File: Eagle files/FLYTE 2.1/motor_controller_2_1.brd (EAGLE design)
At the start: 80 x 60 mm, 32 parts, among them J1 XT60-M, U1 MIC29302WU-TRTO-263-5_MCH-M

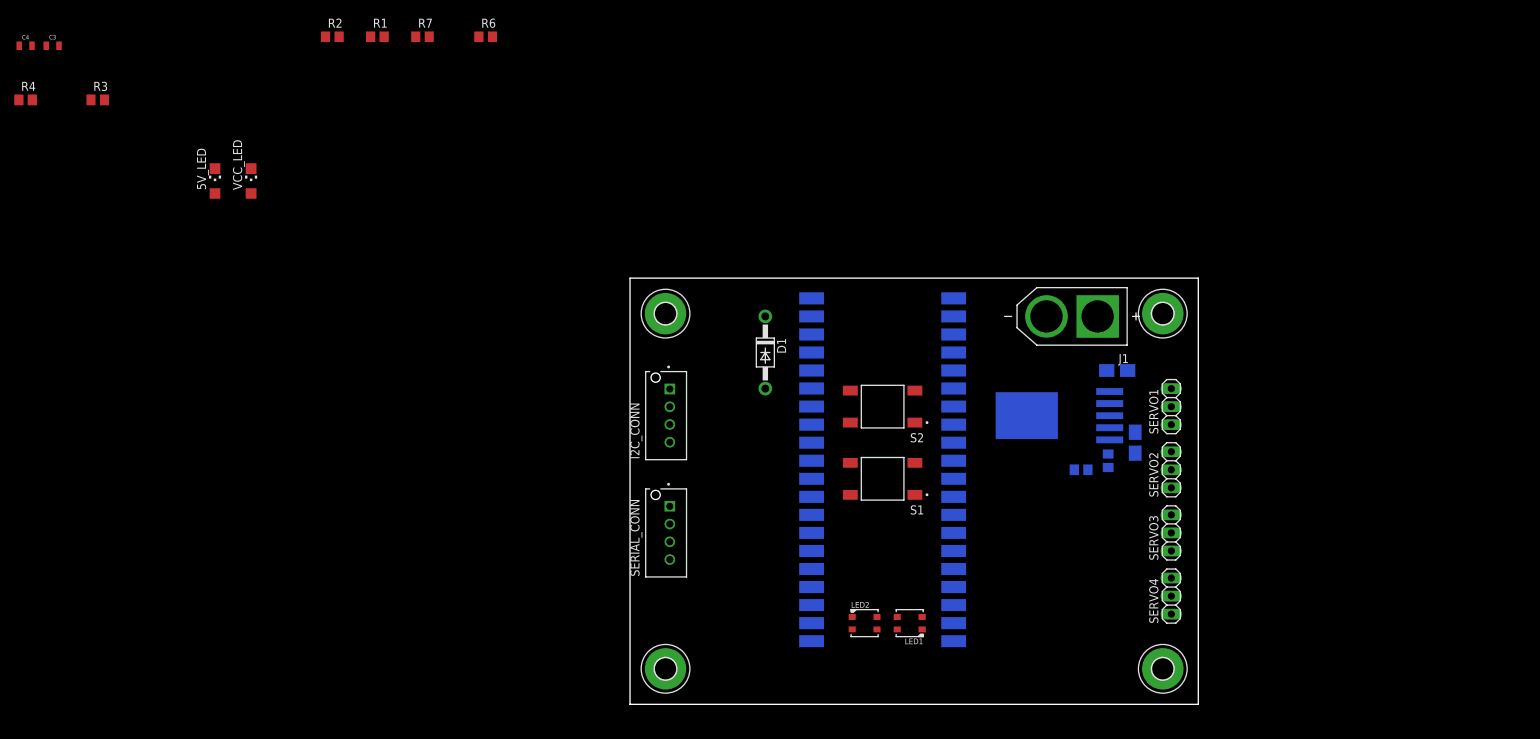
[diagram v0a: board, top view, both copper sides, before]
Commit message: Schematics of FC and motor controller
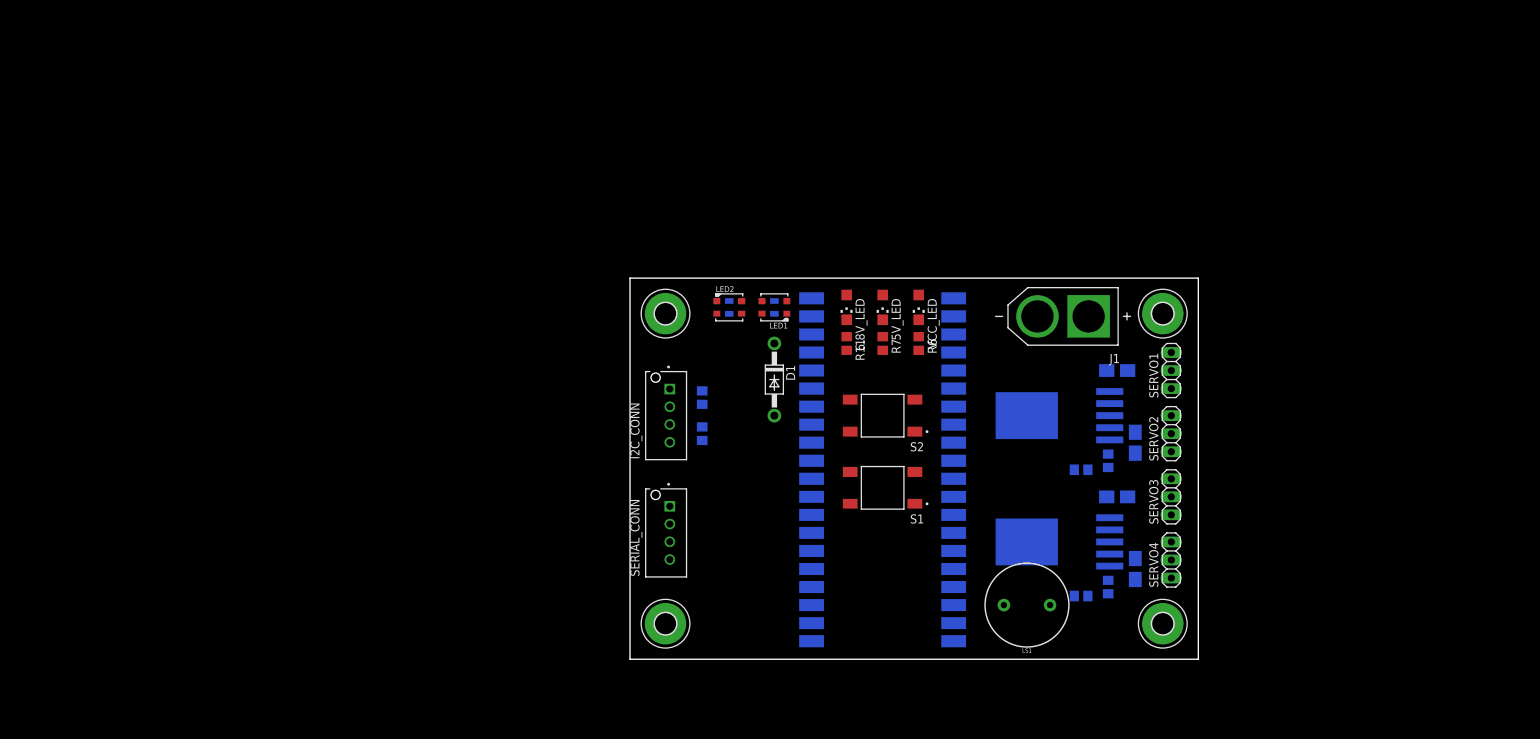
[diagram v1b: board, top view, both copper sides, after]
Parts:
- removed R1, R2: 100k, rcl:R0805
- added 6.8V_LED: (no value), adafruit:CHIPLED_1206
- added C5, C6: 10 uF, microbuilder:EIA3216-18/A-W
- added LS1: BUZZER-PTH, SparkFun-Electromechanical:BUZZER-12MM
- added R10: 442k ohm, rcl:R0805
- added R11: 330 ohm, rcl:R0805
- added R5: 100k ohm, rcl:R0805
- added U2: MIC29302WU-TRTO-263-5_MCH-M, MIC29302WU:TO-263-5_MCH-M
- moved C3 108.1 mm to (20.3, 55.9), flipped to the bottom, turned to 270 degrees
- moved C4 105.7 mm to (14.0, 55.9), flipped to the bottom, turned to 90 degrees
- moved R4 104.1 mm to (10.2, 43.2), flipped to the bottom, turned to 90 degrees
- moved R3 97.2 mm to (10.2, 38.1), flipped to the bottom, turned to 270 degrees
- moved 5V_LED 95.6 mm to (35.6, 55.9), turned to 180 degrees
- moved VCC_LED 95.6 mm to (40.6, 55.9), turned to 180 degrees
- moved R7 77.8 mm to (35.6, 50.8), turned to 270 degrees
- moved R6 74.7 mm to (40.6, 50.8), turned to 270 degrees
- moved LED1 48.4 mm to (20.3, 55.9)
- moved LED2 48.4 mm to (14.0, 55.9)
- moved H3 6.35 mm to (5.00, 11.3)
- moved H4 6.35 mm to (75.0, 11.3)
- moved SERVO1 5.08 mm to (76.2, 47.0)
- moved SERVO3 5.08 mm to (76.2, 29.2)
- moved SERVO4 5.08 mm to (76.2, 20.3)
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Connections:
- removed net N$4: PICO.P$34, R1.2, R2.2
- new net 6.8V: 6.8V_LED.A, C6.+, R10.2, SERVO1.2, SERVO2.2, SERVO3.2, SERVO4.2, U2.4
- new net BUZZER: LS1.+, PICO.P$14
- new net N$5: R10.1, R5.1, U2.5
- new net N$8: 6.8V_LED.C, R11.1
- net 5V: no longer R2.1
- net 7.4V: now also C5.+, U2.1, U2.2; no longer SERVO1.2, SERVO2.2, SERVO3.2, SERVO4.2
- net GND: now also C5.-, C6.-, LS1.-, R11.2, R5.2, U1.6, U2.3, U2.6; no longer R1.1, R4.1
- net SDA0: now also R4.1
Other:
- board size 80 x 60 mm -> 80 x 53.6 mm

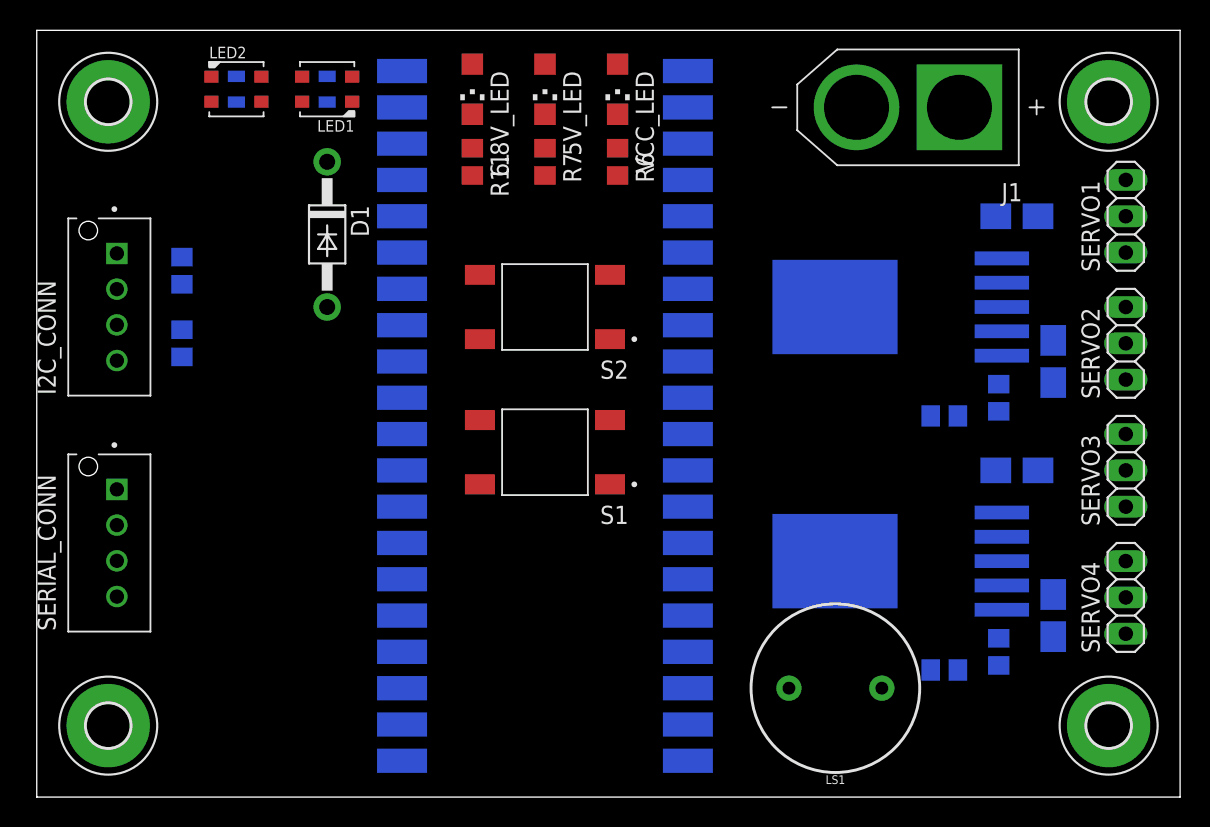
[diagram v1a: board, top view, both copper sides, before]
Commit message: payload sch 408 mc board
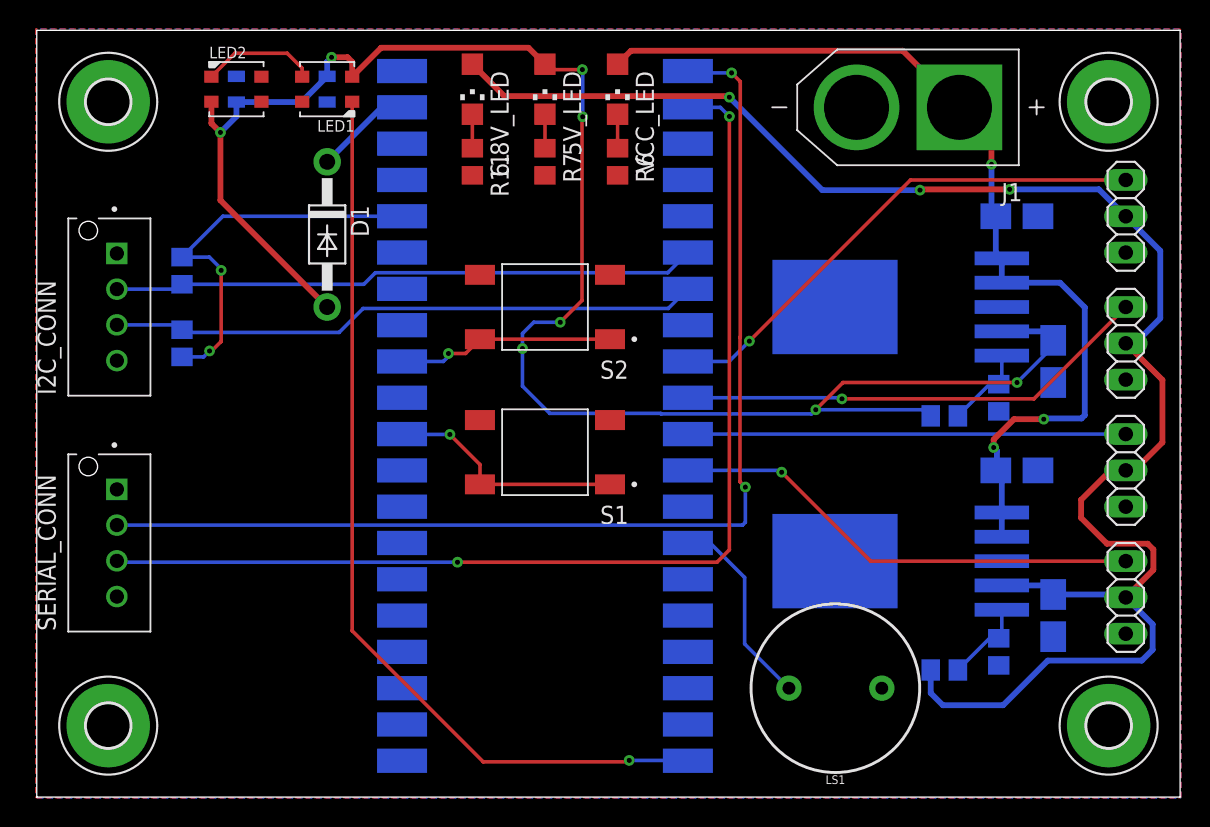
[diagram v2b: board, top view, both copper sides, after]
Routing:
- net 5V: track 0.00 -> 126.4 mm, vias 0 -> 8
- net 6.8V: track 0.00 -> 120.8 mm, vias 0 -> 3
- net SER_TX: track 0.00 -> 79.0 mm, vias 0 -> 2
- net SER_RX: track 0.00 -> 76.7 mm, vias 0 -> 2
- net 7.4V: track 0.00 -> 67.7 mm, vias 0 -> 3
- net LED: track 0.00 -> 65.7 mm, vias 0 -> 1
- net SCL0: track 0.00 -> 41.4 mm
- net SDA0: track 0.00 -> 41.0 mm
- net SERVO1: track 0.00 -> 35.9 mm, vias 0 -> 1
- net SERVO2: track 0.00 -> 33.3 mm, vias 0 -> 1
- net SERVO4: track 0.00 -> 33.3 mm, vias 0 -> 1
- net SERVO3: track 0.00 -> 30.6 mm
- net 3V3: track 0.00 -> 28.0 mm, vias 0 -> 2
- net N$2: track 0.00 -> 16.8 mm, vias 0 -> 1
- net N$3: track 0.00 -> 15.3 mm, vias 0 -> 1
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- added copper zone on layer 1, net GND
- added copper zone on layer 16, net GND

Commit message: motor controller v2.1
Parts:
- removed S1, S2: TS04-66-95-BK-100-SMT, TS04-66-95-BK-100-SMT:SW_TS04-66-95-BK-100-SMT
- removed SERVO1, SERVO2, SERVO3, SERVO4: (no value), pinhead:1X03
- added INTERFACE, RESET: TS04-66-95-BK-100-SMT, TS04-66-95-BK-100-SMT:SW_TS04-66-95-BK-100-SMT
- added J2, J3, J4, J5: S3B-XH-A(LF)(SN), S3B-XH-A_LF__SN_:JST_S3B-XH-A(LF)(SN)
- added U$1: (no value), servo1_label:SERVO10
- added U$10: (no value), tx_label:TX0
- added U$11: (no value), lipo_2s_label:LIPO_2S0
- added U$12: (no value), 5v_label:5V0
- added U$13: (no value), 7v4_label:7V40
- added U$14: (no value), 6v8_label:6V80
- added U$15: (no value), status_label:STATUS0
- added U$16: (no value), motor_controller_label:MOTOR_CONTROLLER0
- added U$2: (no value), servo2_label:SERVO20
- added U$3: (no value), servo3_label:SERVO30
- added U$4: (no value), servo4_label:SERVO40
- added U$5: (no value), sda_label:SDA0
- added U$6: (no value), scl_label:SCL0
- added U$7, U$8: (no value), gnd_label:GND0
- added U$9: (no value), rx_label:RX0
- moved C4 80.0 mm to (73.4, 2.29)
- moved LED2 80.0 mm to (73.4, 2.29)
- moved C3 80.0 mm to (79.8, 2.29)
- moved LED1 80.0 mm to (79.8, 2.29)
- moved H3 51.4 mm to (55.5, 2.21)
- moved H2 50.6 mm to (55.5, 53.5)
- moved I2C_CONN 49.3 mm to (54.4, 39.1)
- moved SERIAL_CONN 49.3 mm to (54.4, 22.6)
- moved R3 49.3 mm to (59.4, 36.6)
- moved R4 49.3 mm to (59.4, 41.7)
- moved H4 47.0 mm to (121.1, 2.21)
- moved H1 46.1 mm to (121.1, 53.5)
- moved D1 43.1 mm to (63.2, 49.8)
- moved LS1 42.4 mm to (97.5, 6.10)
- moved PICO 41.7 mm to (78.5, 30.2)
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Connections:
- net 6.8V: now also J2.2, J3.2, J4.2, J5.2; no longer SERVO1.2, SERVO2.2, SERVO3.2, SERVO4.2
- net GND: now also INTERFACE.2, INTERFACE.4, J2.1, J3.1, J4.1, J5.1, RESET.2, RESET.4; no longer S1.2, S1.4, S2.2, S2.4, SERVO1.1, SERVO2.1, SERVO3.1, SERVO4.1
- net N$2: now also RESET.1, RESET.3; no longer S1.1, S1.3
- net N$3: now also INTERFACE.1, INTERFACE.3; no longer S2.1, S2.3
- net SERVO1: now also J2.3; no longer SERVO1.3
- net SERVO2: now also J3.3; no longer SERVO2.3
- net SERVO3: now also J4.3; no longer SERVO3.3
- net SERVO4: now also J5.3; no longer SERVO4.3
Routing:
- net LED: track 65.7 -> 9.28 mm
- net 5V: track 126.4 -> 139.9 mm, vias 8 -> 7
- net 6.8V: track 120.8 -> 109.6 mm
- net 3V3: track 28.0 -> 18.6 mm
- net SDA0: track 41.0 -> 33.4 mm
- net SCL0: track 41.4 -> 33.8 mm
- net SER_RX: track 76.7 -> 69.1 mm
- net SER_TX: track 79.0 -> 71.6 mm
- net BUZZER: track 14.0 -> 20.4 mm
- net SERVO2: track 33.3 -> 30.6 mm
- net N$1: track 6.82 -> 4.71 mm
- net SERVO4: track 33.3 -> 34.9 mm
- net N$14: track 5.92 -> 7.44 mm
- net SERVO1: track 35.9 -> 34.9 mm
- net SERVO3: track 30.6 -> 31.6 mm, vias 0 -> 1
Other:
- board size 80 x 53.6 mm -> 75.6 x 61.3 mm
- board text added: "R10"

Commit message: flyte done
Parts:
- 5V_LED, 6.8V_LED, VCC_LED: device adafruit:CHIPLED_1206 -> led:CHIPLED_1206

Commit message: .
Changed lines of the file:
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@@
 </layers>
 <board>
-<fusionsync huburn="a.YnVzaW5lc3M6aWl0YjUzNQ" projecturn="a.YnVzaW5lc3M6aWl0YjUzNSNEMjAyMjA3MjU1NDIwMjEzNzY" f3durn="urn:adsk.wipprod:dm.lineage:8IMc14VtSl-5fDwUJquSpw" pcbguid="" lastpulledtime="" lastsyncedchangeguid="" latestrevisionid="a0f8438c-b738-4322-bdc5-6236827b66e7" lastsyncedrevisionid="a0f8438c-b738-4322-bdc5-6236827b66e7" lastboardhashguid="21d1f3f7-0f8b-bc3e-4432-33a0da882c0f" lastpushedtime="2024-05-08T04:04:01Z" linktopcb3d="true"/>
+<fusionsync huburn="a.YnVzaW5lc3M6aWl0YjUzNQ" projecturn="a.YnVzaW5lc3M6aWl0YjUzNSNEMjAyMjA3MjU1NDIwMjEzNzY" f3durn="urn:adsk.wipprod:dm.lineage:8IMc14VtSl-5fDwUJquSpw" pcbguid="" lastpulledtime="" lastsyncedchangeguid="" latestrevisionid="a0f8438c-b738-4322-bdc5-6236827b66e7" lastsyncedrevisionid="a0f8438c-b738-4322-bdc5-6236827b66e7" lastboardhashguid="21d1f3f7-0f8b-bc3e-4432-33a0da882c0f" lastpushedtime="2024-05-08T04:04:01Z" linktopcb3d="false"/>
 <plain>
 <wire x1="50.546" y1="-2.794" x2="126.101" y2="-2.794" width="0" layer="20"/>
@@
 <wire x1="72.136" y1="52.606" x2="72.136" y2="50.226" width="0.254" layer="1"/>
 </signal>
+<signal name="N$4">
+<via x="60.198" y="9.906" extent="1-16" drill="0.35"/>
+</signal>
+<signal name="N$6">
+<via x="76.962" y="12.573" extent="1-16" drill="0.35"/>
+</signal>
+<signal name="N$11">
+<via x="108.585" y="2.667" extent="1-16" drill="0.35"/>
+</signal>
+<signal name="N$12">
+<via x="107.442" y="8.382" extent="1-16" drill="0.35"/>
+</signal>
+<signal name="N$13">
+<via x="92.202" y="45.72" extent="1-16" drill="0.35"/>
+</signal>
+<signal name="N$15">
+<via x="115.062" y="51.816" extent="1-16" drill="0.35"/>
+</signal>
+<signal name="N$16">
+<via x="75.057" y="44.196" extent="1-16" drill="0.35"/>
+</signal>
+<signal name="N$17">
+<via x="63.627" y="1.524" extent="1-16" drill="0.35"/>
+</signal>
 </signals>

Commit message: .
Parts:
- moved R6 50.6 mm to (31.7, 52.1)
- moved VCC_LED 50.6 mm to (31.7, 57.2)
- moved C4 50.6 mm to (22.9, 5.09)
- moved D1 50.6 mm to (12.7, 52.6)
- moved I2C_CONN 50.6 mm to (3.81, 41.9)
- moved LED2 50.6 mm to (22.9, 5.09)
- moved LS1 50.6 mm to (47.0, 8.90)
- moved PICO 50.6 mm to (27.9, 33.0)
- moved SERIAL_CONN 50.6 mm to (3.81, 25.4)
- moved U$11 50.6 mm to (43.4, 50.6)
- moved U$13 50.6 mm to (33.8, 55.1)
- moved U$15 50.6 mm to (22.1, 8.90)
- moved 5V_LED 50.6 mm to (26.7, 57.2)
- moved 6.8V_LED 50.6 mm to (21.6, 57.2)
- moved C1 50.6 mm to (58.4, 48.3)
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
